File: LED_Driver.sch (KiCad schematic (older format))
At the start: 0 parts

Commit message: 3.8 Understanding The LED Driver Module
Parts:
- added C? (x2): C, ~, symbol C
- added D?: DIODESCH, ~, symbol DIODESCH
- added L?: INDUCTOR, ~, symbol INDUCTOR
- added R?: R, ~, symbol R
- added U?: AP5726, symbol AP5726
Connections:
- net String+: now also C?.1, D?.2 (K), U?.5 (OVP)
- net String-: now also U?.3 (FB)
- new net: D?.1 (A), L?.2, U?.1 (SW)
- new net +5V: C?.1, L?.1, U?.6 (VIN)
- new net GND: C?.2, C?.2, R?.2, U?.2 (GND)
- new net LED_EN_PWM: U?.4 (EN)
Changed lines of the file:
@@
 LIBS:BenchBudEE
 LIBS:BenchBudEE-cache
-EELAYER 24 0
+EELAYER 27 0
 EELAYER END
 $Descr A4 11693 8268
@@
 Sheet 5 9
 Title ""
-Date "7 feb 2014"
+Date "8 feb 2014"
 Rev ""
 Comp ""
@@
 $EndDescr
 Text HLabel 2300 2400 0    60   Input ~ 0
-En
-Text HLabel 2300 2600 0    60   Input ~ 0
-FREQ
-Text HLabel 5300 2400 0    60   Input ~ 0
+LED_EN_PWM
+Text HLabel 9200 1250 2    60   Input ~ 0
 String+
-Text HLabel 5300 2600 0    60   Output ~ 0
+Text HLabel 9200 2750 2    60   Output ~ 0
 String-
+$Comp
+L AP5726 U?
+U 1 1 52F721D4
+P 4250 2500
+F 0 "U?" H 4700 1850 60  0000 C CNN
+F 1 "AP5726" H 4250 2500 60  0000 C CNN
+F 2 "" H 4250 2500 60  0000 C CNN
+F 3 "" H 4250 2500 60  0000 C CNN
+	1    4250 2500
+	1    0    0    -1
+$EndComp
+Wire Wire Line
+	2300 2400 3450 2400
+$Comp
+L GND #PWR?
+U 1 1 52F721EF
+P 4250 3950
+F 0 "#PWR?" H 4250 3950 30  0001 C CNN
+F 1 "GND" H 4250 3880 30  0001 C CNN
+F 2 "" H 4250 3950 60  0000 C CNN
+F 3 "" H 4250 3950 60  0000 C CNN
+	1    4250 3950
+	1    0    0    -1
+$EndComp
+Wire Wire Line
+	4250 3350 4250 3650
+Wire Wire Line
+	4250 3650 4250 3950
+$Comp
+L +5V #PWR?
+U 1 1 52F72EB7
+P 3100 1050
+F 0 "#PWR?" H 3100 1140 20  0001 C CNN
+F 1 "+5V" H 3100 1140 30  0000 C CNN
+F 2 "" H 3100 1050 60  0000 C CNN
+F 3 "" H 3100 1050 60  0000 C CNN
+	1    3100 1050
+	1    0    0    -1
+$EndComp
+$Comp
+L GND #PWR?
+U 1 1 52F72EC4
+P 3100 2000
+F 0 "#PWR?" H 3100 2000 30  0001 C CNN
+F 1 "GND" H 3100 1930 30  0001 C CNN
+F 2 "" H 3100 2000 60  0000 C CNN
+F 3 "" H 3100 2000 60  0000 C CNN
+	1    3100 2000
+	1    0    0    -1
+$EndComp
+$Comp
+L C C?
+U 1 1 52F72ECC
+P 3100 1550
+F 0 "C?" H 3100 1650 40  0000 L CNN
+F 1 "C" H 3106 1465 40  0000 L CNN
+F 2 "~" H 3138 1400 30  0000 C CNN
+F 3 "~" H 3100 1550 60  0000 C CNN
+	1    3100 1550
+	1    0    0    -1
+$EndComp
+Wire Wire Line
+	3100 1050 3100 1250
+Wire Wire Line
+	3100 1250 3100 1350
+Wire Wire Line
+	3100 1750 3100 2000
+Wire Wire Line
+	3100 1250 3600 1250
+Wire Wire Line
+	3600 1250 3900 1250
+Connection ~ 3100 1250
+$Comp
+L C C?
+U 1 1 52F72EF9
+P 8450 1750
+F 0 "C?" H 8450 1850 40  0000 L CNN
+F 1 "C" H 8456 1665 40  0000 L CNN
+F 2 "~" H 8488 1600 30  0000 C CNN
+F 3 "~" H 8450 1750 60  0000 C CNN
+	1    8450 1750
+	1    0    0    -1
+$EndComp
+$Comp
+L INDUCTOR L?
+U 1 1 52F72F01
+P 4200 1250
+F 0 "L?" V 4150 1250 40  0000 C CNN
+F 1 "INDUCTOR" V 4300 1250 40  0000 C CNN
+F 2 "~" H 4200 1250 60  0000 C CNN
+F 3 "~" H 4200 1250 60  0000 C CNN
+	1    4200 1250
+	0    -1   -1   0
+$EndComp
+Wire Wire Line
+	4750 1600 4500 1600
+$Comp
+L DIODESCH D?
+U 1 1 52F72F21
+P 5250 1250
+F 0 "D?" H 5250 1350 40  0000 C CNN
+F 1 "DIODESCH" H 5250 1150 40  0000 C CNN
+F 2 "~" H 5250 1250 60  0000 C CNN
+F 3 "~" H 5250 1250 60  0000 C CNN
+	1    5250 1250
+	1    0    0    -1
+$EndComp
+Wire Wire Line
+	4500 1250 4750 1250
+Wire Wire Line
+	4750 1250 5050 1250
+Wire Wire Line
+	5450 1250 5850 1250
+Wire Wire Line
+	5850 1250 8450 1250
+Wire Wire Line
+	8450 1250 9200 1250
+Wire Wire Line
+	8450 1250 8450 1550
+Wire Wire Line
+	3950 1600 3600 1600
+Wire Wire Line
+	3600 1600 3600 1250
+Connection ~ 3600 1250
+Wire Wire Line
+	4750 1600 4750 1250
+Connection ~ 4750 1250
+Connection ~ 8450 1250
+Wire Wire Line
+	5050 2750 9200 2750
+$Comp
+L R R?
+U 1 1 52F72F95
+P 5450 3000
+F 0 "R?" V 5530 3000 40  0000 C CNN
+F 1 "R" V 5457 3001 40  0000 C CNN
+F 2 "~" V 5380 3000 30  0000 C CNN
+F 3 "~" H 5450 3000 30  0000 C CNN
+	1    5450 3000
+	1    0    0    -1
+$EndComp
+Wire Wire Line
+	5450 3250 5450 3650
+Wire Wire Line
+	5450 3650 4250 3650
+Connection ~ 4250 3650
+Wire Wire Line
+	5050 2400 5850 2400
+Wire Wire Line
+	5850 2400 5850 1250
+Connection ~ 5850 1250
+$Comp
+L GND #PWR?
+U 1 1 52F72FE8
+P 8450 2250
+F 0 "#PWR?" H 8450 2250 30  0001 C CNN
+F 1 "GND" H 8450 2180 30  0001 C CNN
+F 2 "" H 8450 2250 60  0000 C CNN
+F 3 "" H 8450 2250 60  0000 C CNN
+	1    8450 2250
+	1    0    0    -1
+$EndComp
+Wire Wire Line
+	8450 1950 8450 2250
 $EndSCHEMATC

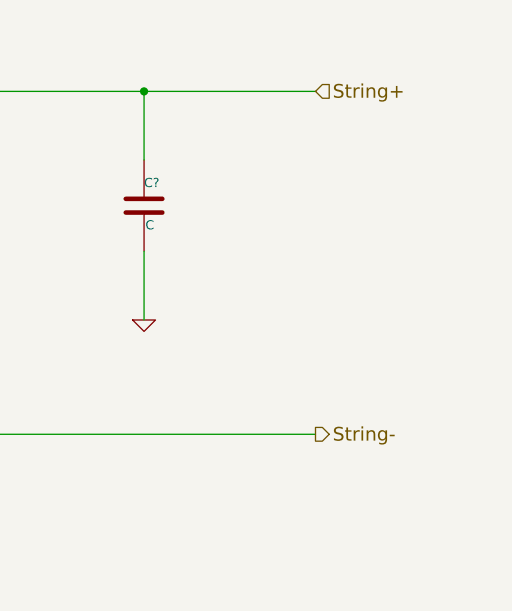
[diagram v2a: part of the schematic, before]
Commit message: 3.9 Understanding The Arduino Module Added content to Arduino and block (header) modules
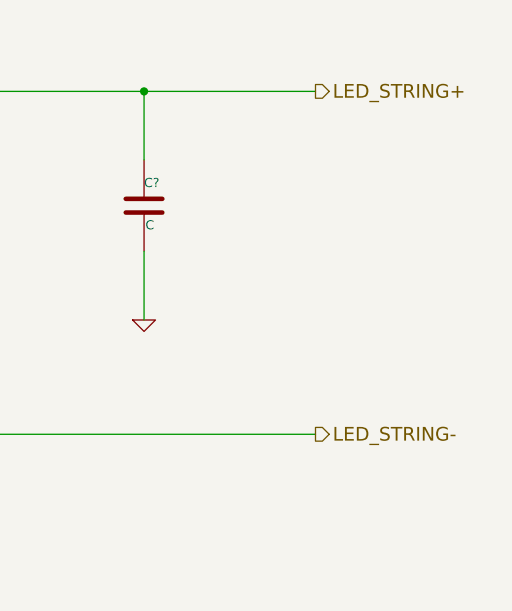
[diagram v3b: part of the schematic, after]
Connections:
- net String+ renamed LED_STRING+
- net String- renamed LED_STRING-
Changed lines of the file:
@@
 Sheet 5 9
 Title ""
-Date "8 feb 2014"
+Date "10 feb 2014"
 Rev ""
 Comp ""
@@
 Text HLabel 2300 2400 0    60   Input ~ 0
 LED_EN_PWM
-Text HLabel 9200 1250 2    60   Input ~ 0
-String+
+Text HLabel 9200 1250 2    60   Output ~ 0
+LED_STRING+
 Text HLabel 9200 2750 2    60   Output ~ 0
-String-
+LED_STRING-
 $Comp
 L AP5726 U?

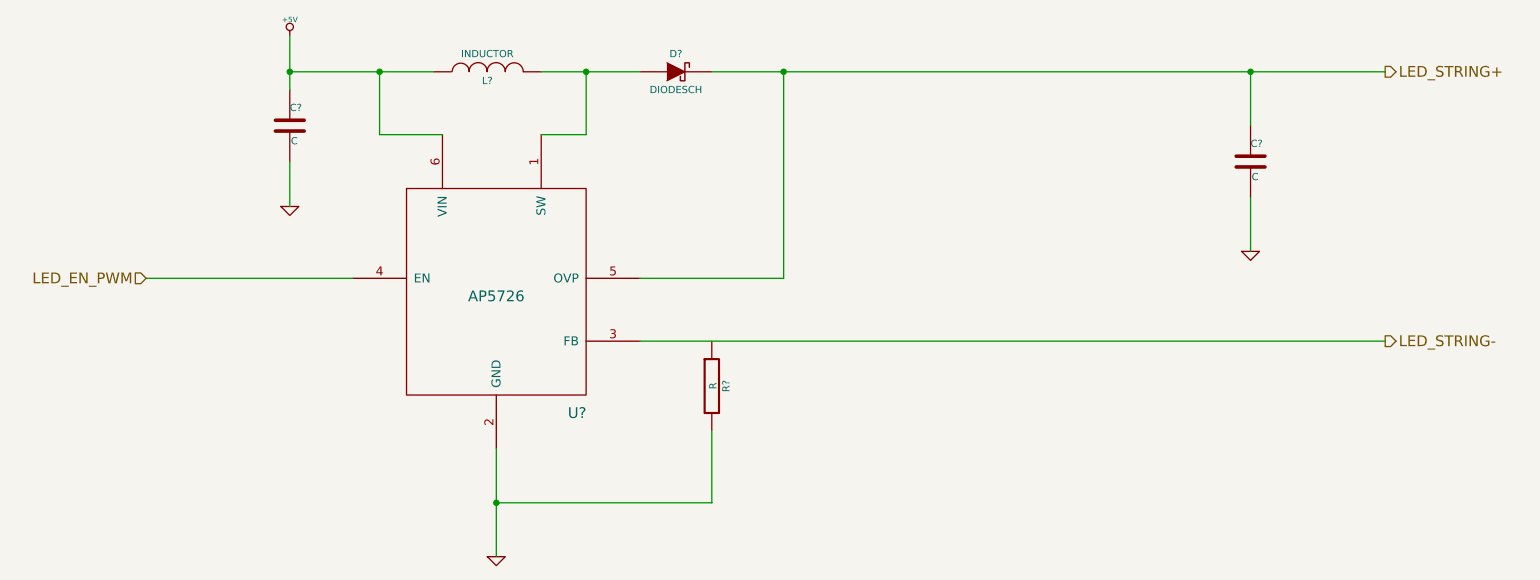
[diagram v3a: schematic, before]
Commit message: 5.3 Video 1/2 Associating and Placing the Relay Module
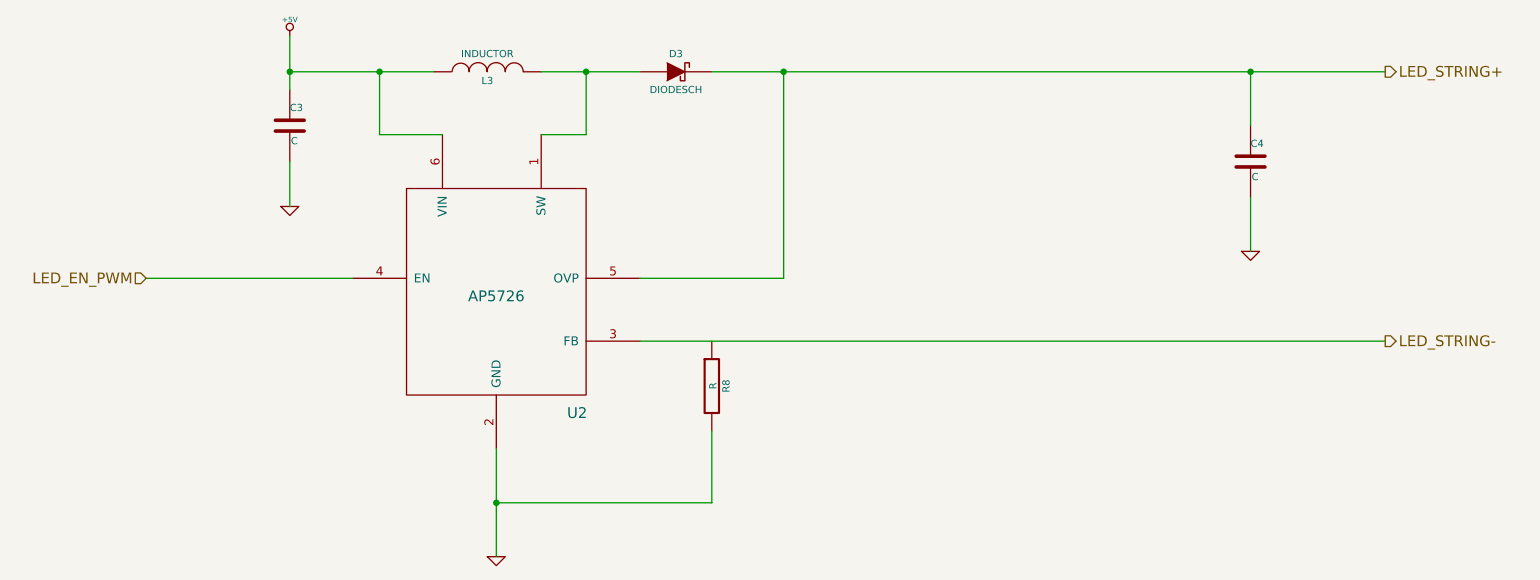
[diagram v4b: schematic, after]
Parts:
- gave numbers to parts that had none: 6
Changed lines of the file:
@@
 Sheet 5 9
 Title ""
-Date "10 feb 2014"
+Date "19 feb 2014"
 Rev ""
 Comp ""
@@
 LED_STRING-
 $Comp
-L AP5726 U?
+L AP5726 U2
 U 1 1 52F721D4
 P 4250 2500
-F 0 "U?" H 4700 1850 60  0000 C CNN
+F 0 "U2" H 4700 1850 60  0000 C CNN
 F 1 "AP5726" H 4250 2500 60  0000 C CNN
 F 2 "" H 4250 2500 60  0000 C CNN
@@
 	2300 2400 3450 2400
 $Comp
-L GND #PWR?
+L GND #PWR016
 U 1 1 52F721EF
 P 4250 3950
-F 0 "#PWR?" H 4250 3950 30  0001 C CNN
+F 0 "#PWR016" H 4250 3950 30  0001 C CNN
 F 1 "GND" H 4250 3880 30  0001 C CNN
 F 2 "" H 4250 3950 60  0000 C CNN
@@
 $EndComp
 Wire Wire Line
-	4250 3350 4250 3650
-Wire Wire Line
-	4250 3650 4250 3950
+	4250 3350 4250 3950
 $Comp
-L +5V #PWR?
+L +5V #PWR017
 U 1 1 52F72EB7
 P 3100 1050
-F 0 "#PWR?" H 3100 1140 20  0001 C CNN
+F 0 "#PWR017" H 3100 1140 20  0001 C CNN
 F 1 "+5V" H 3100 1140 30  0000 C CNN
 F 2 "" H 3100 1050 60  0000 C CNN
@@
 $EndComp
 $Comp
-L GND #PWR?
+L GND #PWR018
 U 1 1 52F72EC4
 P 3100 2000
-F 0 "#PWR?" H 3100 2000 30  0001 C CNN
+F 0 "#PWR018" H 3100 2000 30  0001 C CNN
 F 1 "GND" H 3100 1930 30  0001 C CNN
 F 2 "" H 3100 2000 60  0000 C CNN
@@
 $EndComp
 $Comp
-L C C?
+L C C3
 U 1 1 52F72ECC
 P 3100 1550
-F 0 "C?" H 3100 1650 40  0000 L CNN
+F 0 "C3" H 3100 1650 40  0000 L CNN
 F 1 "C" H 3106 1465 40  0000 L CNN
 F 2 "~" H 3138 1400 30  0000 C CNN
@@
 $EndComp
 Wire Wire Line
-	3100 1050 3100 1250
-Wire Wire Line
-	3100 1250 3100 1350
+	3100 1050 3100 1350
 Wire Wire Line
 	3100 1750 3100 2000
 Wire Wire Line
-	3100 1250 3600 1250
-Wire Wire Line
-	3600 1250 3900 1250
+	3100 1250 3900 1250
 Connection ~ 3100 1250
 $Comp
-L C C?
+L C C4
 U 1 1 52F72EF9
 P 8450 1750
-F 0 "C?" H 8450 1850 40  0000 L CNN
+F 0 "C4" H 8450 1850 40  0000 L CNN
 F 1 "C" H 8456 1665 40  0000 L CNN
 F 2 "~" H 8488 1600 30  0000 C CNN
@@
 $EndComp
 $Comp
-L INDUCTOR L?
+L INDUCTOR L3
 U 1 1 52F72F01
 P 4200 1250
-F 0 "L?" V 4150 1250 40  0000 C CNN
+F 0 "L3" V 4150 1250 40  0000 C CNN
 F 1 "INDUCTOR" V 4300 1250 40  0000 C CNN
 F 2 "~" H 4200 1250 60  0000 C CNN
@@
 	4750 1600 4500 1600
 $Comp
-L DIODESCH D?
+L DIODESCH D3
 U 1 1 52F72F21
 P 5250 1250
-F 0 "D?" H 5250 1350 40  0000 C CNN
+F 0 "D3" H 5250 1350 40  0000 C CNN
 F 1 "DIODESCH" H 5250 1150 40  0000 C CNN
 F 2 "~" H 5250 1250 60  0000 C CNN
@@
 $EndComp
 Wire Wire Line
-	4500 1250 4750 1250
+	4500 1250 5050 1250
 Wire Wire Line
-	4750 1250 5050 1250
-Wire Wire Line
-	5450 1250 5850 1250
-Wire Wire Line
-	5850 1250 8450 1250
-Wire Wire Line
-	8450 1250 9200 1250
+	5450 1250 9200 1250
 Wire Wire Line
 	8450 1250 8450 1550
@@
 	5050 2750 9200 2750
 $Comp
-L R R?
+L R R8
 U 1 1 52F72F95
 P 5450 3000
-F 0 "R?" V 5530 3000 40  0000 C CNN
+F 0 "R8" V 5530 3000 40  0000 C CNN
 F 1 "R" V 5457 3001 40  0000 C CNN
 F 2 "~" V 5380 3000 30  0000 C CNN
@@
 Connection ~ 5850 1250
 $Comp
-L GND #PWR?
+L GND #PWR019
 U 1 1 52F72FE8
 P 8450 2250
-F 0 "#PWR?" H 8450 2250 30  0001 C CNN
+F 0 "#PWR019" H 8450 2250 30  0001 C CNN
 F 1 "GND" H 8450 2180 30  0001 C CNN
 F 2 "" H 8450 2250 60  0000 C CNN
